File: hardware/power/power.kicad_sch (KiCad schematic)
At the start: 38 parts, among them J2 Conn_01x04_Pin, J4 Conn_01x04_Pin, P1 USB_C_Plug_USB2.0, U2 ESP32-S3-WROOM-1, U4 MCP1825S

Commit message: swapped imu, minor changes, renaming
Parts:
- removed MPU6000: ~, 0_stuff:QFN24_4X4X0P9_IVS, symbol 0_pwrmtr:MPU6050
- added ICM-42670-P1: ~, Package_LGA:LGA-14_3x2.5mm_P0.5mm_LayoutBorder3x4y, symbol 0_pwrmtr:ICM-42670-P
- C1: value 100n -> 10n
- C10: value 1u -> 2.2u
- C2: value 2.2n -> 0.1u
- D4: value D -> 1N400X
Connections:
- net +3V3: now also C1.2, C2.2, ICM-42670-P1.5 (VDDIO), ICM-42670-P1.8 (VDD)
- net CLK_{ADC}: now also U2.9 (IO16); no longer U2.10 (IO17)
- net CS_{ADC}: now also U2.14 (IO20); no longer U2.15 (IO3)
- net CS_{gyro}: now also U2.8 (IO15), ICM-42670-P1.12 (CS); no longer U2.7 (IO7)
- net DRDY_{ADC}: now also U2.13 (IO19); no longer U2.14 (IO20)
- net GND: now also ICM-42670-P1.6 (GND), ICM-42670-P1.7 (FSYNC)
- net LED_{1}: now also U2.35 (IO42)
- net LED_{2}: now also U2.34 (IO41)
- net MISO: now also U2.11 (IO18), ICM-42670-P1.1 (SDO); no longer U2.12 (IO8)
- net MOSI: now also U2.10 (IO17), ICM-42670-P1.14 (SDI); no longer U2.11 (IO18)
- net RX: now also U2.24 (IO47); no longer U2.26 (IO45)
- net SCLK: now also U2.12 (IO8), ICM-42670-P1.13 (SCLK); no longer U2.13 (IO19)
- net SHDN_{CAN}: now also U2.25 (IO48); no longer U2.27 (IO0)
- net STB_{CAN}: now also U2.26 (IO45); no longer U2.28 (IO35)
- net SYNC_{ADC}: now also U2.15 (IO3); no longer U2.16 (IO46)
- net TX: now also U2.23 (IO21); no longer U2.25 (IO48)
- net INT_{gyro} renamed INT1_{gyro}
- net INT1_{gyro}: now also ICM-42670-P1.4 (INT)
- net LED: no longer names the net of U2.4 (IO4)
- net LED: no longer U2.35 (IO42)
- new net INT2_{gyro}: ICM-42670-P1.9 (INT2), U2.7 (IO7)

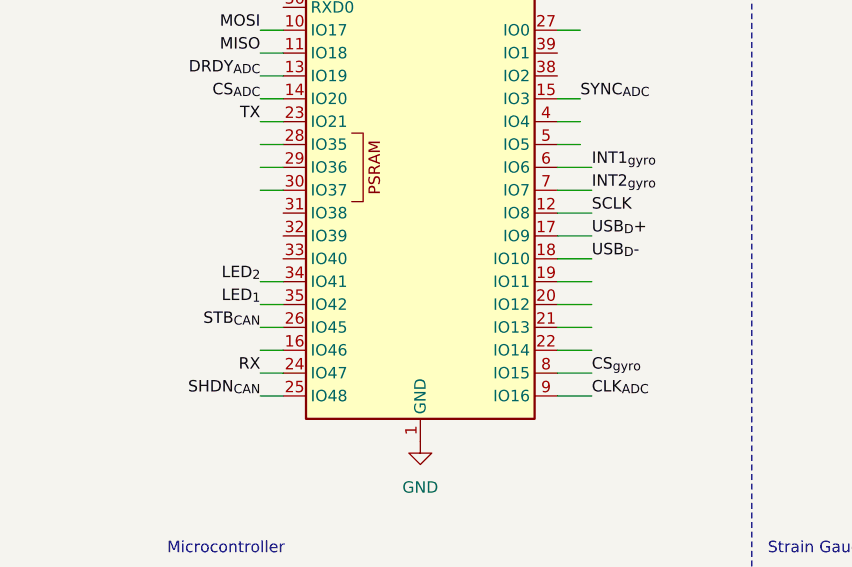
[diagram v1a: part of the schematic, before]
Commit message: redid some traces
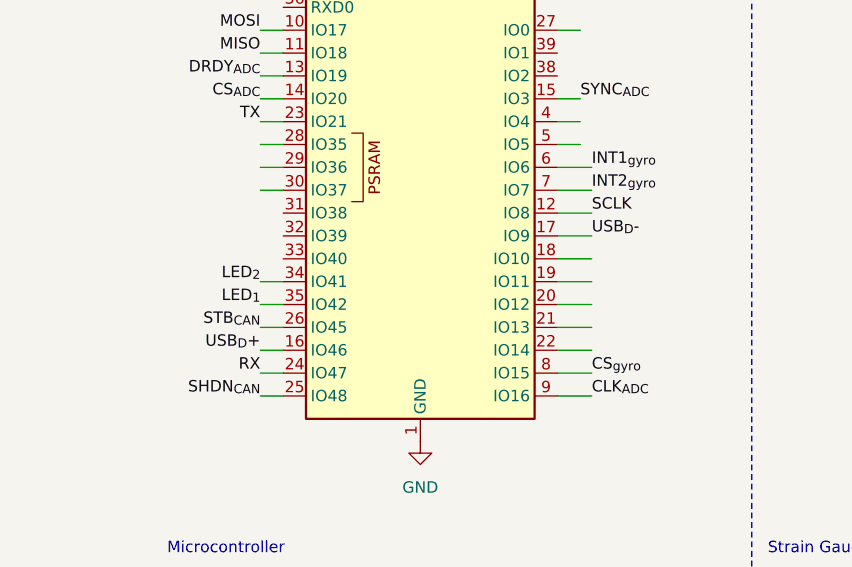
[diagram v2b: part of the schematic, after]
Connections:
- net USB_{D}+: now also U2.16 (IO46); no longer U2.17 (IO9)
- net USB_{D}-: now also U2.17 (IO9); no longer U2.18 (IO10)
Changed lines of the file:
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@@
-		)
-	)
-	(label "USB_{D}+"
-		(at 62.23 69.85 0)
-		(fields_autoplaced yes)
-		(effects
-			(font
-				(size 1.27 1.27)
-			)
-			(justify left bottom)
 		)
 	)
@@
 		)
 	)
+	(label "USB_{D}+"
+		(at 25.4 82.55 180)
+		(fields_autoplaced yes)
+		(effects
+			(font
+				(size 1.27 1.27)
+			)
+			(justify right bottom)
+		)
+	)
 	(label "ADS-"
 		(at 116.84 30.48 0)
@@
 		)
 	)
+	(label "USB_{D}-"
+		(at 62.23 69.85 0)
+		(fields_autoplaced yes)
+		(effects
+			(font
+				(size 1.27 1.27)
+			)
+			(justify left bottom)
+		)
+	)
 	(label "CS_{ADC}"
 		(at 25.4 54.61 180)
@@
 		)
 	)
-	(label "USB_{D}-"
-		(at 62.23 72.39 0)
-		(fields_autoplaced yes)
-		(effects
-			(font
-				(size 1.27 1.27)
-			)
-			(justify left bottom)
-		)
-	)
